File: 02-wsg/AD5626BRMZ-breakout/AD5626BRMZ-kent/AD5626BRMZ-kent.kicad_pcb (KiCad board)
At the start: 2 copper layers, 5 parts, among them J1 Conn_01x04, J2 Conn_01x04, U1 AD5626BRMZ

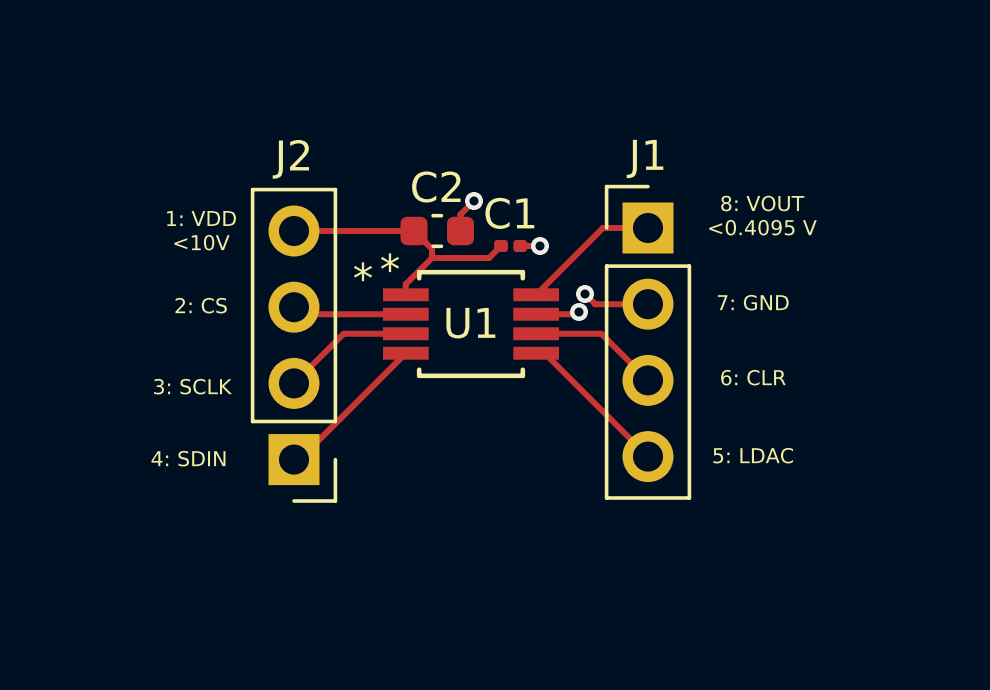
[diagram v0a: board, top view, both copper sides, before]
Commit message: updated breakout
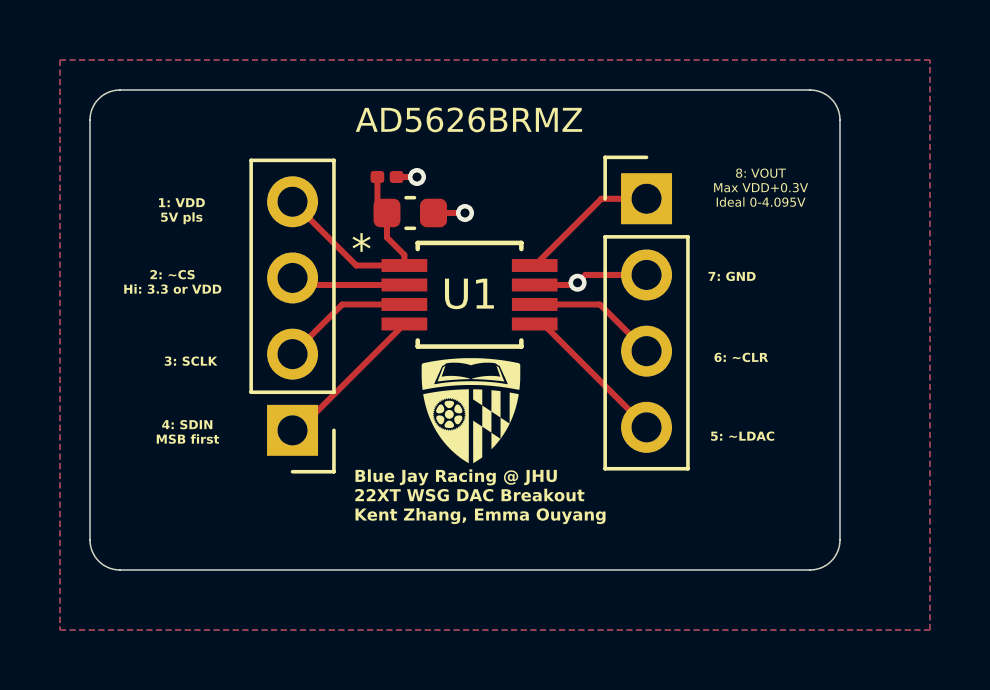
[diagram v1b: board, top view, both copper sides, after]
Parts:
- added G***: BJR_LOGO, BJR_LOGO, F.Cu at (138.7, 99.7)
- added G***: BJR_LOGO, BJR_LOGO, B.Cu at (138.7, 99.7)
- moved 0.1uF 4.72 mm to (135.9, 91.9)
- moved 10uF 1.08 mm to (136.7, 93.1)
- moved J2 0.98 mm to (132.8, 100.3)
- moved J1 0.98 mm to (144.6, 92.6)
- moved U1 0.98 mm to (138.7, 95.8)
- renumbered C1 to 0.1uF, C2 to 10uF
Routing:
- net Net-(J2-Pin_4): track 9.20 -> 7.93 mm
- net GND_C: track 6.16 -> 6.07 mm, vias 4 -> 3
- added copper zone on B.Cu, net GND_C
- added copper zone on F.Cu, net GND_C
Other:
- board outline added: 25 x 16 mm
- board text added: "1: VDD 5V pls"
- board text added: "2: ~CS Hi: 3.3 or VDD"
- board text added: "4: SDIN MSB first"
- board text added: "5: ~LDAC"
- board text added: "6: ~CLR"
- board text added: "8: VOUT Max VDD+0.3V Ideal 0-4.095V"
- board text added: "Blue Jay Racing @ JHU 22XT WSG DAC Breakout Kent Zhang, Emma Ouyang"
- board text removed: "1: VDD <10V"
- board text removed: "2: CS"
- board text removed: "4: SDIN"
- board text removed: "5: LDAC"
- board text removed: "6: CLR"
- board text removed: "8: VOUT <0.4095 V"

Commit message: made pins breadboard-compatible, aligned capacitors, shrunk overall board size
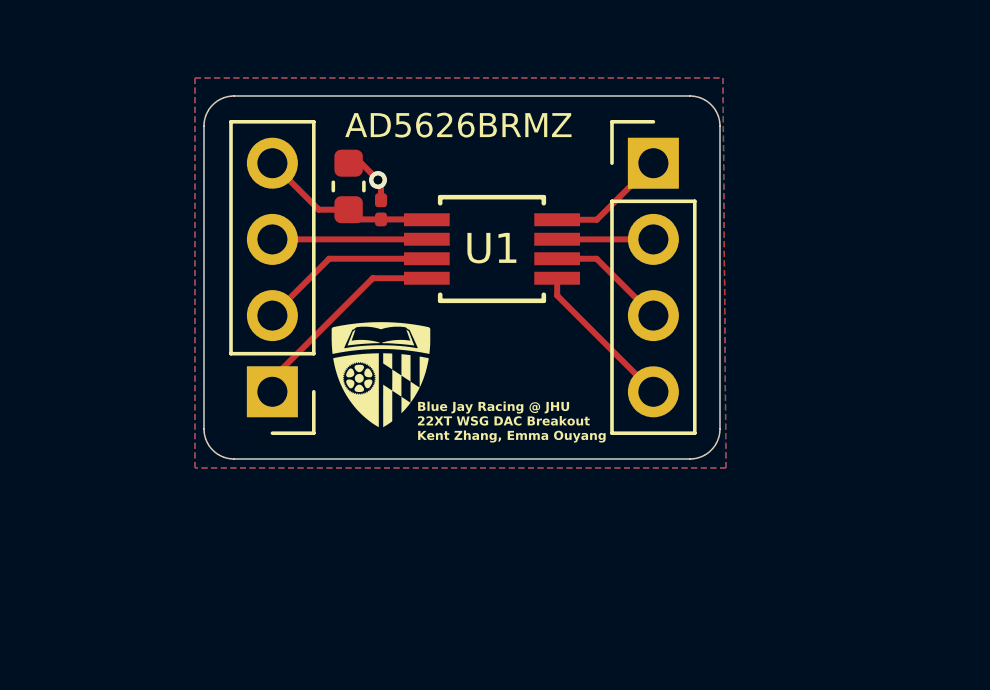
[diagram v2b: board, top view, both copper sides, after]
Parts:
- moved G*** 3.23 mm to (135.7, 98.5)
- moved 10uF 2.24 mm to (134.6, 92.2), turned to 90 degrees
- moved U1 1.70 mm to (139.4, 94.3)
- moved J2 1.45 mm to (132.1, 99.1)
- moved G*** 1.39 mm to (138.0, 98.5)
- moved J1 1.21 mm to (144.8, 91.4)
- moved 0.1uF 1.11 mm to (135.7, 93.0), turned to 90 degrees
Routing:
- net Net-(J2-Pin_4): track 7.93 -> 5.93 mm
- net Net-(J2-Pin_1): track 5.20 -> 6.97 mm
- net Net-(J2-Pin_2): track 4.41 -> 5.93 mm
- net Net-(J2-Pin_3): track 3.83 -> 5.15 mm
- net GND_C: track 6.07 -> 5.14 mm, vias 3 -> 1
- net Net-(J1-Pin_1): track 4.65 -> 3.99 mm
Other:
- board size 25 x 16 mm -> 17.2 x 12.1 mm
- board text added: "5: ~LDAC Serial Reg Data -> DAC Register"
- board text removed: "5: ~LDAC"

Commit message: swapped ground fill zone to back copper layer
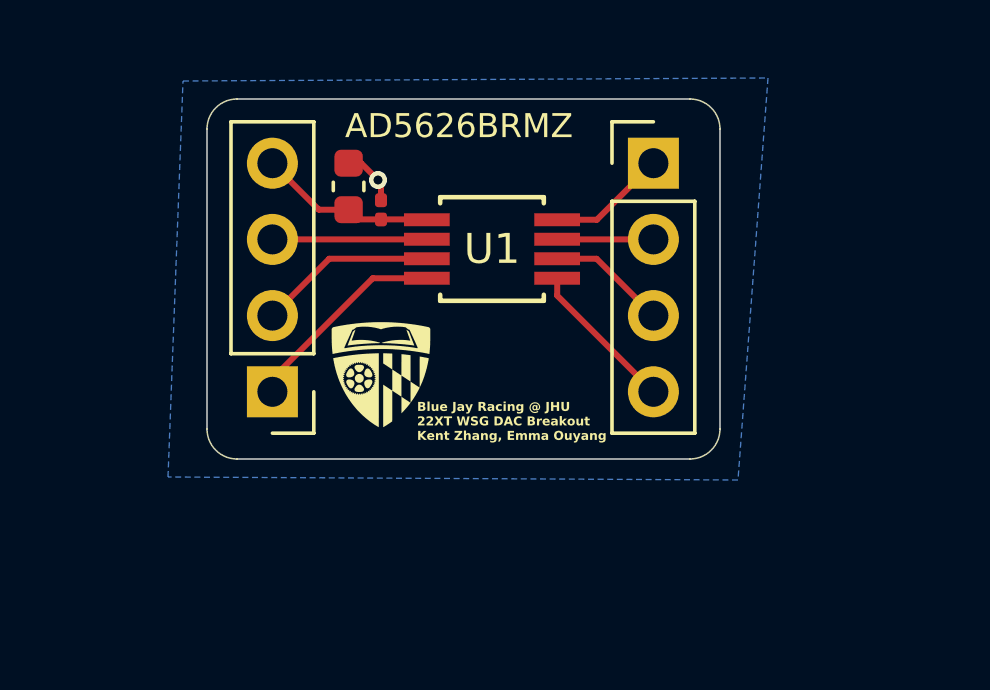
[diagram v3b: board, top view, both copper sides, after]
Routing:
- removed copper zone on F.Cu, net GND_C
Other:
- board size 17.2 x 12.1 mm -> 17.1 x 12 mm
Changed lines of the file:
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@@
-	)
-	(gr_arc
-		(start 130.8 101.3)
-		(mid 130.092893 101.007107)
-		(end 129.8 100.3)
-		(stroke
-			(width 0.05)
-			(type default)
-		)
-		(layer "Edge.Cuts")
 	)
 	(gr_arc
@@
 	)
 	(gr_line
-		(start 130.8 89.2)
-		(end 146 89.2)
+		(start 129.9 100.3)
+		(end 129.9 90.3)
+		(stroke
+			(width 0.05)
+			(type default)
+		)
+		(layer "Edge.Cuts")
+	)
+	(gr_line
+		(start 130.9 89.3)
+		(end 146 89.3)
 		(stroke
 			(width 0.05)
@@
 	)
 	(gr_arc
-		(start 146 89.2)
-		(mid 146.707107 89.492893)
-		(end 147 90.2)
+		(start 129.9 90.3)
+		(mid 130.192893 89.592893)
+		(end 130.9 89.3)
+		(stroke
+			(width 0.05)
+			(type default)
+		)
+		(layer "Edge.Cuts")
+	)
+	(gr_line
+		(start 147 90.3)
+		(end 147 100.3)
 		(stroke
 			(width 0.05)
@@
 	)
 	(gr_arc
-		(start 129.8 90.2)
-		(mid 130.092893 89.492893)
-		(end 130.8 89.2)
+		(start 146 89.3)
+		(mid 146.707107 89.592893)
+		(end 147 90.3)
+		(stroke
+			(width 0.05)
+			(type default)
+		)
+		(layer "Edge.Cuts")
+	)
+	(gr_arc
+		(start 130.9 101.3)
+		(mid 130.192893 101.007107)
+		(end 129.9 100.3)
 		(stroke
 			(width 0.05)
@@
 	(gr_line
 		(start 146 101.3)
-		(end 130.8 101.3)
-		(stroke
-			(width 0.05)
-			(type default)
-		)
-		(layer "Edge.Cuts")
-	)
-	(gr_line
-		(start 129.8 100.3)
-		(end 129.8 90.2)
-		(stroke
-			(width 0.05)
-			(type default)
-		)
-		(layer "Edge.Cuts")
-	)
-	(gr_line
-		(start 147 90.2)
-		(end 147 100.3)
+		(end 130.9 101.3)
 		(stroke
 			(width 0.05)
@@
 		(net 8)
 		(net_name "GND_C")
-		(layers "F.Cu" "B.Cu")
+		(layer "B.Cu")
 		(hatch edge 0.5)
 		(connect_pads yes
@@
 		(polygon
 			(pts
-				(xy 129.5 88.6) (xy 147.1 88.6) (xy 147.2 101.6) (xy 129.5 101.6)
-			)
-		)
+				(xy 129.1 88.7) (xy 148.6 88.6) (xy 147.6 102) (xy 128.6 101.9)
+			)
+		)

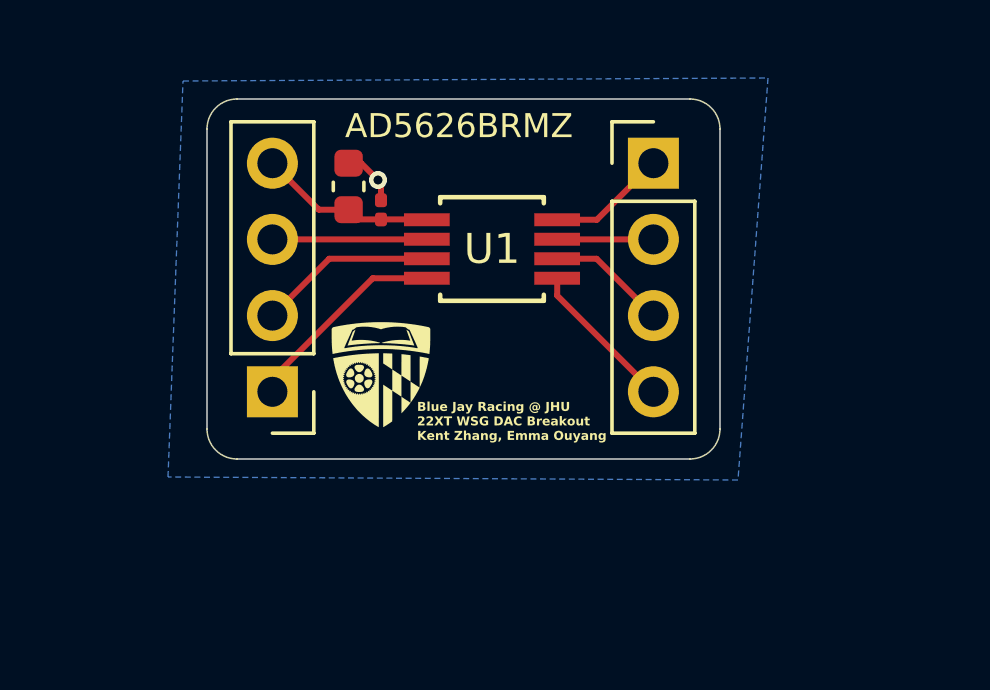
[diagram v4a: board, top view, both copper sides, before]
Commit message: Added additionally ground pour to wsg dac & added thermal relief to gnd net
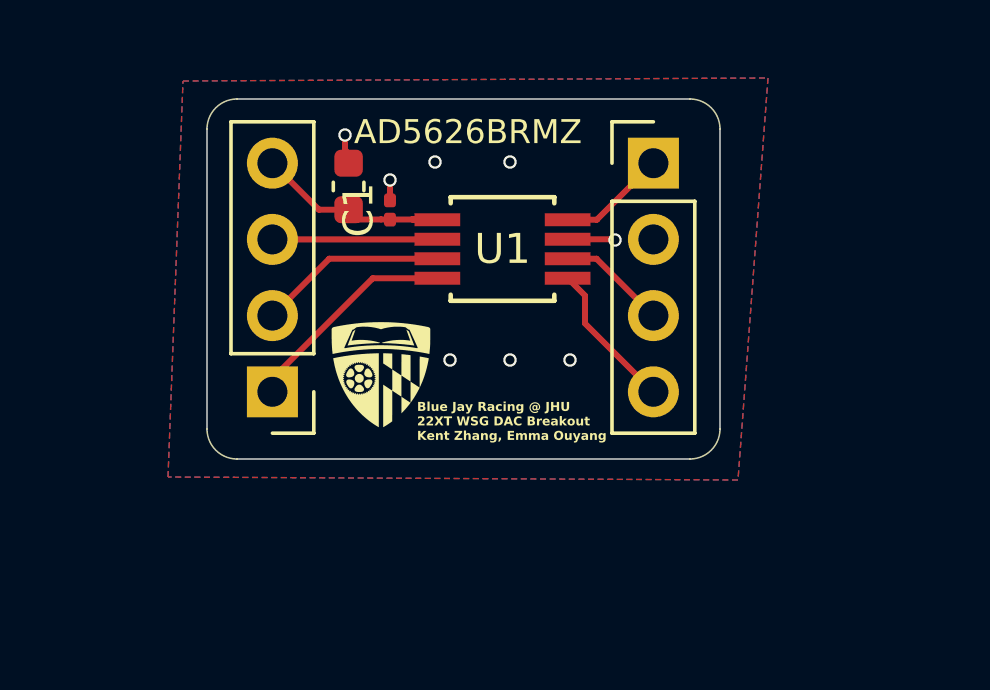
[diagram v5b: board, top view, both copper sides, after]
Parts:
- moved U1 0.35 mm to (139.8, 94.3)
- moved C1 0.30 mm to (136.0, 93.0)
- renumbered 0.1uF to C1, 10uF to C2
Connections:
- net GND_C renamed GND
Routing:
- net GND: track 5.14 -> 3.10 mm, vias 1 -> 8
- net Net-(J2-Pin_4): track 5.93 -> 6.76 mm
- added copper zone on F.Cu, net GND
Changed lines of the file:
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@@
 	(net 6 "Net-(J2-Pin_1)")
 	(net 7 "Net-(J2-Pin_4)")
-	(net 8 "GND_C")
+	(net 8 "GND")
 	(footprint "Connector_PinHeader_2.54mm:PinHeader_1x04_P2.54mm_Vertical"
 		(layer "F.Cu")
@@
 		(descr "Capacitor SMD 0603 (1608 Metric), square (rectangular) end terminal, IPC-7351 nominal, (Body size source: IPC-SM-782 page 76, https://www.pcb-3d.com/wordpress/wp-content/uploads/ipc-sm-782a_amendment_1_and_2.pdf), generated with kicad-footprint-generator")
 		(tags "capacitor")
-		(property "Reference" "10uF"
+		(property "Reference" "C2"
 			(at 0 -1.43 90)
 			(layer "F.SilkS")
@@
 			(layers "F.Cu" "F.Mask" "F.Paste")
 			(roundrect_rratio 0.25)
-			(net 8 "GND_C")
+			(net 8 "GND")
 			(pintype "passive")
 		)
@@
 	(footprint "footprints:RM_8_ADI"
 		(layer "F.Cu")
-		(at 139.4 94.3)
+		(at 139.75 94.3)
 		(tags "AD5626BRMZ ")
 		(property "Reference" "U1"
@@
 		)
 		(property "Value" "AD5626BRMZ"
-			(at -1.1 -4.1 0)
+			(at -1.15 -3.9 0)
 			(unlocked yes)
 			(layer "F.SilkS")
@@
 			(size 1.524 0.4318)
 			(layers "F.Cu" "F.Mask" "F.Paste")
-			(net 8 "GND_C")
+			(net 8 "GND")
 			(pinfunction "GND")
 			(pintype "unspecified")
@@
 	(footprint "Capacitor_SMD:C_0201_0603Metric"
 		(layer "F.Cu")
-		(at 135.7 92.995 90)
+		(at 136 93 90)
 		(descr "Capacitor SMD 0201 (0603 Metric), square (rectangular) end terminal, IPC-7351 nominal, (Body size source: https://www.vishay.com/docs/20052/crcw0201e3.pdf), generated with kicad-footprint-generator")
 		(tags "capacitor")
-		(property "Reference" "0.1uF"
-			(at 0.78 -1.1 90)
+		(property "Reference" "C1"
+			(at 0 -1.05 90)
 			(layer "F.SilkS")
-			(hide yes)
 			(effects
 				(font
-					(size 0.7 0.7)
-					(thickness 0.1)
+					(size 1 1)
+					(thickness 0.15)
 				)
 			)
 		)
 		(property "Value" "0.1uF"
-			(at -0.8 1.25 90)
+			(at 0 1.05 90)
 			(layer "F.Fab")
 			(effects
@@
 			(layers "F.Cu" "F.Mask")
 			(roundrect_rratio 0.25)
-			(net 8 "GND_C")
+			(net 8 "GND")
 			(pintype "passive")
 		)
@@
 			(layers "*.Cu" "*.Mask")
 			(remove_unused_layers no)
-			(net 8 "GND_C")
+			(net 8 "GND")
 			(pinfunction "Pin_2")
 			(pintype "passive")
@@
 	)
 	(segment
-		(start 144.78 99.06)
-		(end 141.5717 95.8517)
+		(start 141.9217 95.274999)
+		(end 142.5 95.853299)
 		(width 0.2)
 		(layer "F.Cu")
@@
 	)
 	(segment
-		(start 141.5717 95.8517)
-		(end 141.5717 95.274999)
+		(start 142.5 95.853299)
+		(end 142.5 96.78)
 		(width 0.2)
 		(layer "F.Cu")
@@
 	)
 	(segment
-		(start 141.5717 93.325001)
-		(end 142.894999 93.325001)
+		(start 142.5 96.78)
+		(end 144.78 99.06)
 		(width 0.2)
 		(layer "F.Cu")
-		(net 2)
+		(net 1)
 	)
 	(segment
@@
 	)
 	(segment
-		(start 141.5717 94.625001)
+		(start 141.9217 93.325001)
+		(end 142.894999 93.325001)
+		(width 0.2)
+		(layer "F.Cu")
+		(net 2)
+	)
+	(segment
+		(start 141.9217 94.625001)
 		(end 142.885001 94.625001)
 		(width 0.2)
@@
 	)
 	(segment
-		(start 132.08 99.06)
-		(end 132.08 98.62)
+		(start 132.08 98.62)
+		(end 135.425001 95.274999)
 		(width 0.2)
 		(layer "F.Cu")
@@
 	)
 	(segment
-		(start 132.08 98.62)
-		(end 135.425001 95.274999)
+		(start 132.08 99.06)
+		(end 132.08 98.62)
 		(width 0.2)
 		(layer "F.Cu")
@@
 	(segment
 		(start 135.425001 95.274999)
-		(end 137.2283 95.274999)
+		(end 137.5783 95.274999)
 		(width 0.2)
 		(layer "F.Cu")
@@
 	)
 	(segment
+		(start 136.75 93.315)
+		(end 137.568299 93.315)
+		(width 0.2)
+		(layer "F.Cu")
+		(net 7)
+	)
+	(segment
 		(start 134.62 92.99)
 		(end 134.945 93.315)
@@
 	(segment
 		(start 135.7 93.315)
-		(end 137.218299 93.315)
+		(end 136.75 93.315)
 		(width 0.2)
 		(layer "F.Cu")
@@
 	)
 	(segment
-		(start 135.7 92.1)
-		(end 135.6 92)
+		(start 137.568299 93.315)
+		(end 137.5783 93.325001)
+		(width 0.2)
+		(layer "F.Cu")
+		(net 7)
+	)
+	(segment
+		(start 136.75 93.315)
+		(end 137.218299 93.315)
+		(width 0.2)
+		(layer "F.Cu")
+		(net 7)
+	)
+	(segment
+		(start 134.5 91)
+		(end 134.62 91.12)
 		(width 0.2)
 		(layer "F.Cu")
@@
 	)
 	(segment
-		(start 134.62 91.44)
-		(end 135.04 91.44)
+		(start 134.62 91.12)
+		(end 134.62 91.44)
 		(width 0.2)
 		(layer "F.Cu")
@@
 	)
 	(segment
-		(start 135.7 92.675)
-		(end 135.7 92.1)
+		(start 141.9217 93.974999)
+		(end 143.474999 93.974999)
 		(width 0.2)
 		(layer "F.Cu")
@@
 	)
 	(segment
-		(start 135.04 91.44)
-		(end 135.6 92)
+		(start 143.474999 93.974999)
+		(end 143.5 94)
 		(width 0.2)
 		(layer "F.Cu")
@@
 	)
 	(segment
-		(start 141.576701 93.98)
-		(end 141.5717 93.974999)
+		(start 136 92.52)
+		(end 136 92)
 		(width 0.2)
 		(layer "F.Cu")
@@
 	)
 	(segment
-		(start 144.78 93.98)
-		(end 141.576701 93.98)
+		(start 134.5 90.5)
+		(end 134.5 91)
 		(width 0.2)
 		(layer "F.Cu")
@@
 	)
 	(via
-		(at 135.6 92)
-		(size 0.6)
+		(at 138 98)
+		(size 0.45)
+		(drill 0.3)
+		(layers "F.Cu" "B.Cu")
+		(net 8)
+	)
+	(via
+		(at 143.5 94)
+		(size 0.45)
+		(drill 0.3)
+		(layers "F.Cu" "B.Cu")
+		(net 8)
+	)
+	(via
+		(at 134.5 90.5)
+		(size 0.45)
+		(drill 0.3)
+		(layers "F.Cu" "B.Cu")
+		(net 8)
+	)
+	(via
+		(at 142 98)
+		(size 0.45)
+		(drill 0.3)
+		(layers "F.Cu" "B.Cu")
+		(net 8)
+	)
+	(via
+		(at 137.5 91.4)
+		(size 0.45)
+		(drill 0.3)
+		(layers "F.Cu" "B.Cu")
+		(net 8)
+	)
+	(via
+		(at 140 98)
+		(size 0.45)
+		(drill 0.3)
+		(layers "F.Cu" "B.Cu")
+		(net 8)
+	)
+	(via
+		(at 136 92)
+		(size 0.45)
+		(drill 0.3)
+		(layers "F.Cu" "B.Cu")
+		(net 8)
+	)
+	(via
+		(at 140 91.4)
+		(size 0.45)
 		(drill 0.3)
 		(layers "F.Cu" "B.Cu")
@@
 	(zone
 		(net 8)
-		(net_name "GND_C")
-		(layer "B.Cu")
+		(net_name "GND")
+		(layers "F.Cu" "B.Cu")
 		(hatch edge 0.5)
-		(connect_pads yes
+		(connect_pads
 			(clearance 0.5)
 		)
